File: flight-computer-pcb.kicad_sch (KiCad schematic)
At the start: 18 parts, among them J1 Battery, M1 Servo, U1 Teensy4.1, U10 U3V16F9, U2 BMP390, U3 BNO055, U4 Pressure Transducer, U5 Ultimate_GPS, U6 Parani-ESD100V2, U7 U3V70F6, U8 S7V8F3, U9 S13V10F5

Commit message: feat: add S13V10F5
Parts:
- U6: footprint FlightComputer:BNO055 -> (none)
- U9: footprint (none) -> FlightComputer:S13V10F5
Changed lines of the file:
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@@
 			)
 		)
-		(property "Footprint" "FlightComputer:BNO055"
+		(property "Footprint" ""
 			(at 233.68 115.57 0)
 			(effects
@@
 			)
 		)
-		(property "Footprint" ""
+		(property "Footprint" "FlightComputer:S13V10F5"
 			(at 125.73 170.18 0)
 			(effects

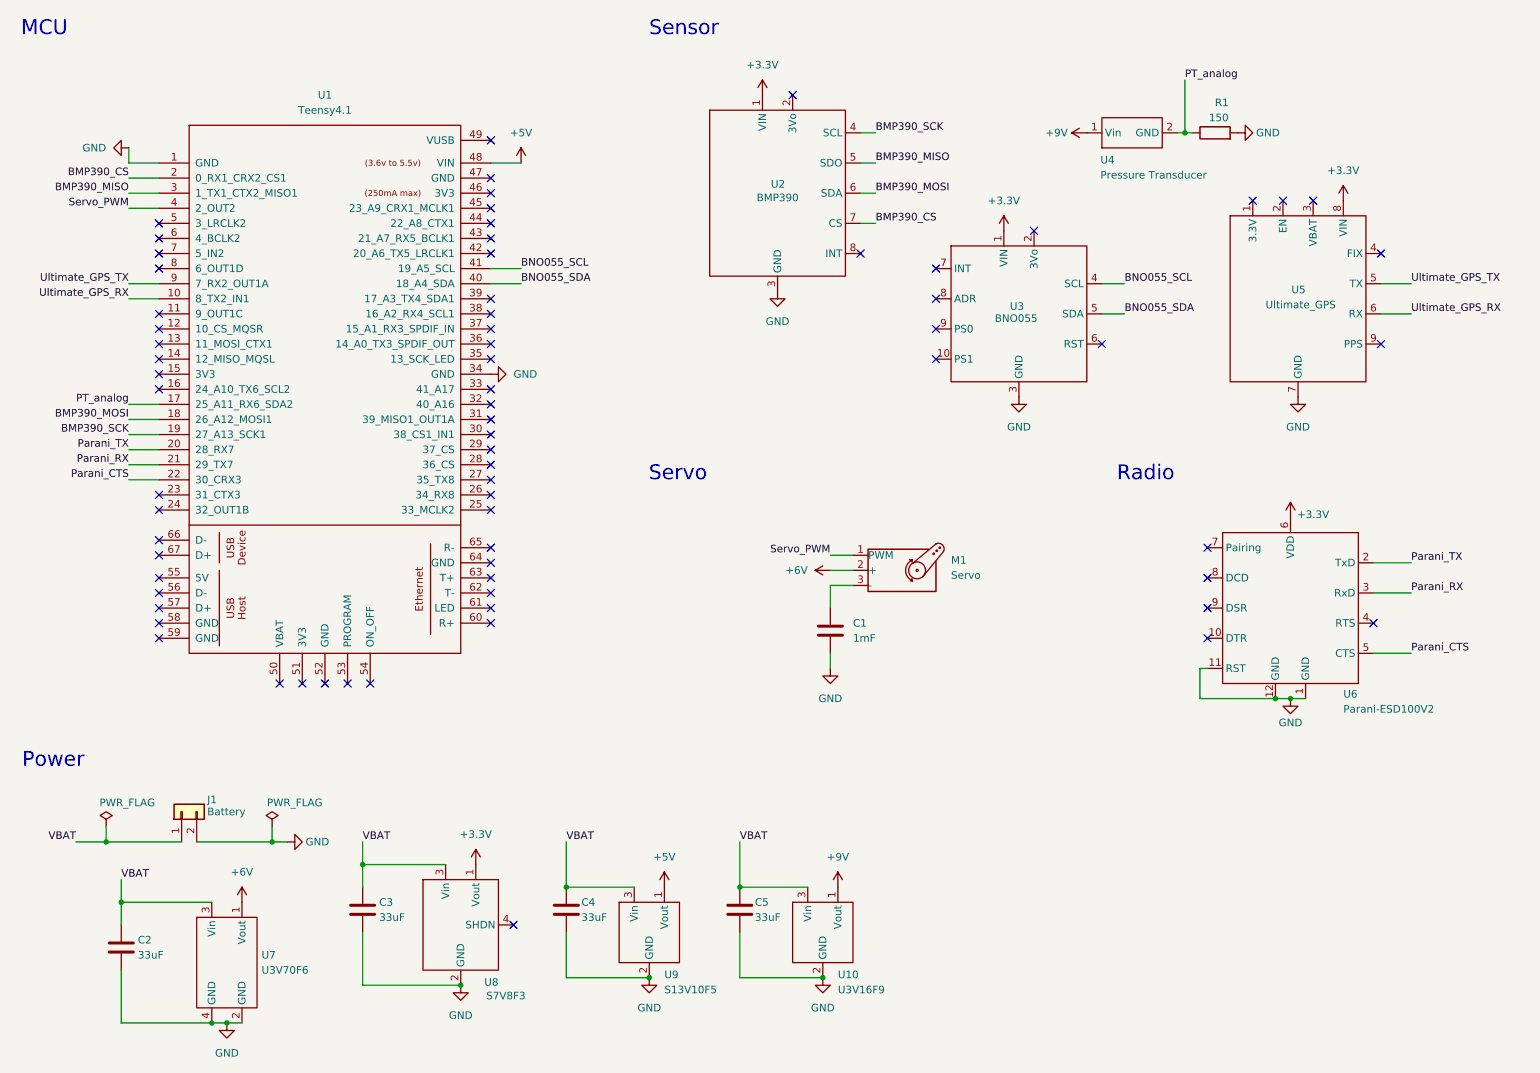
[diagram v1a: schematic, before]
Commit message: feat: add connectors to schematic
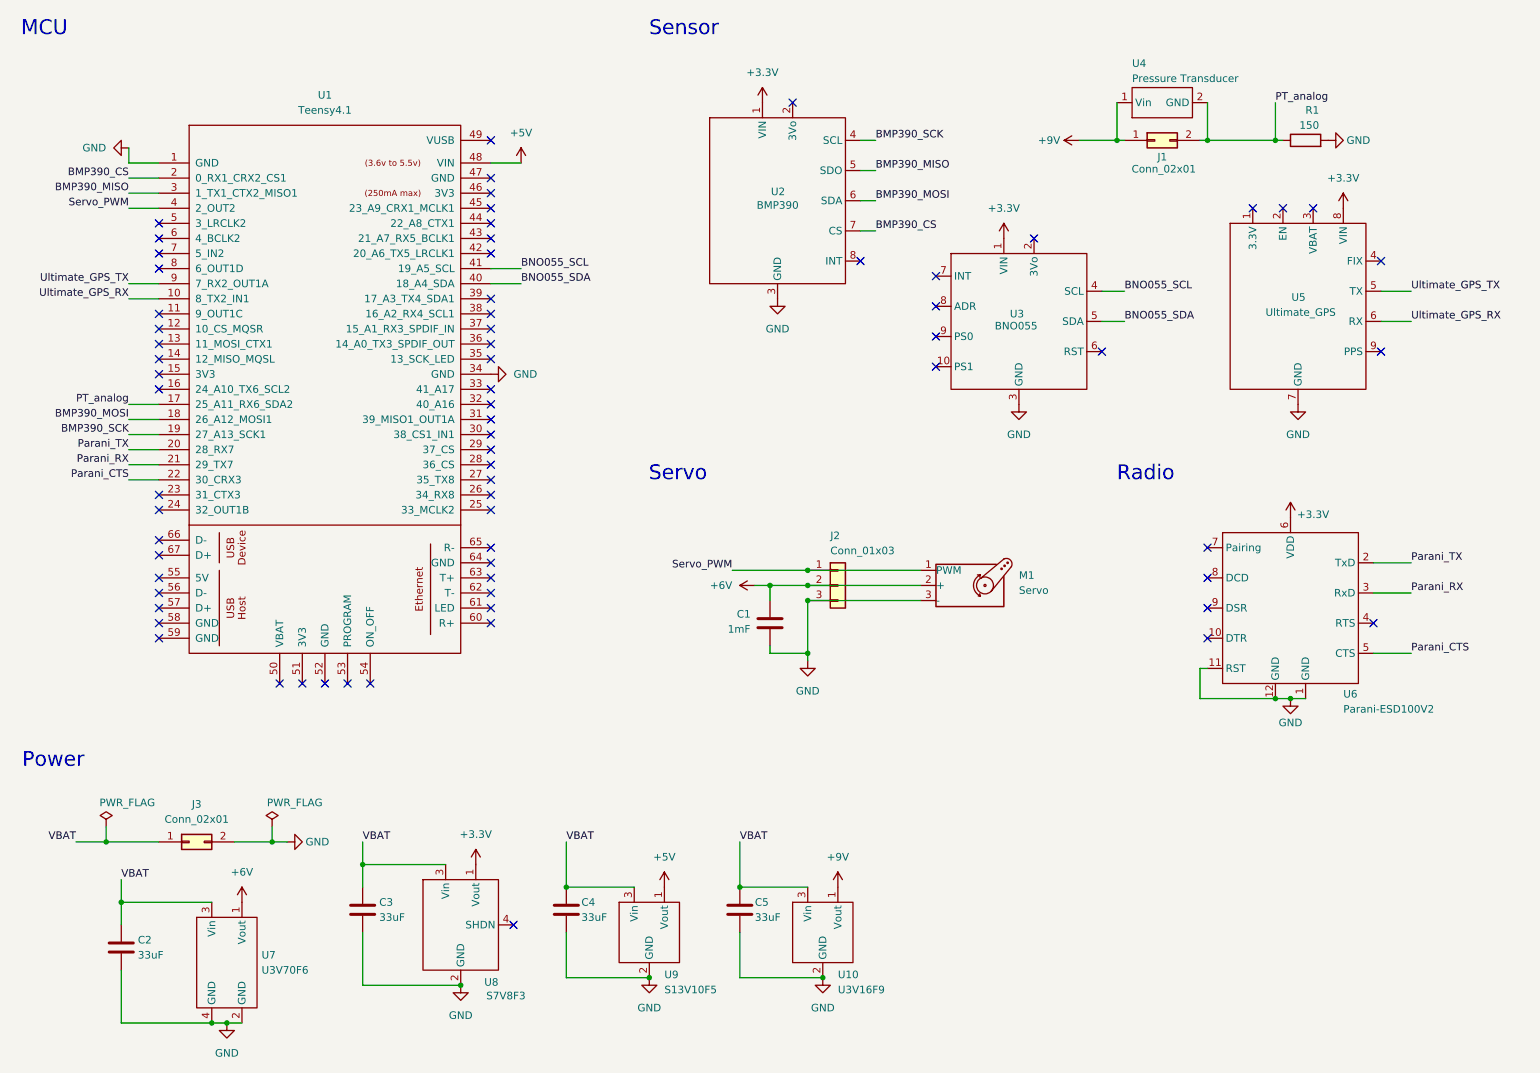
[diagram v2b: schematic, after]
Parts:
- removed J1: Battery, symbol Connector_Generic:Conn_01x02
- added J1, J3: Conn_02x01, symbol Connector_Generic:Conn_02x01
- added J2: Conn_01x03, symbol Connector_Generic:Conn_01x03
- M1, U4: now left out of the parts list
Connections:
- net +6V: now also C1.1, J2.2 (Pin_2)
- net +9V: now also J1.1 (Pin_1)
- net GND: now also M1.3 (-), J2.3 (Pin_3), J3.2 (Pin_2)
- net PT_analog: now also J1.2 (Pin_2)
- net Servo_PWM: now also J2.1 (Pin_1)
- net VBAT: now also J3.1 (Pin_1)
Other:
- moved on the sheet: C1, M1, R1, U2, U3, U4, U5

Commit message: docs: add "external module" comments to schematic
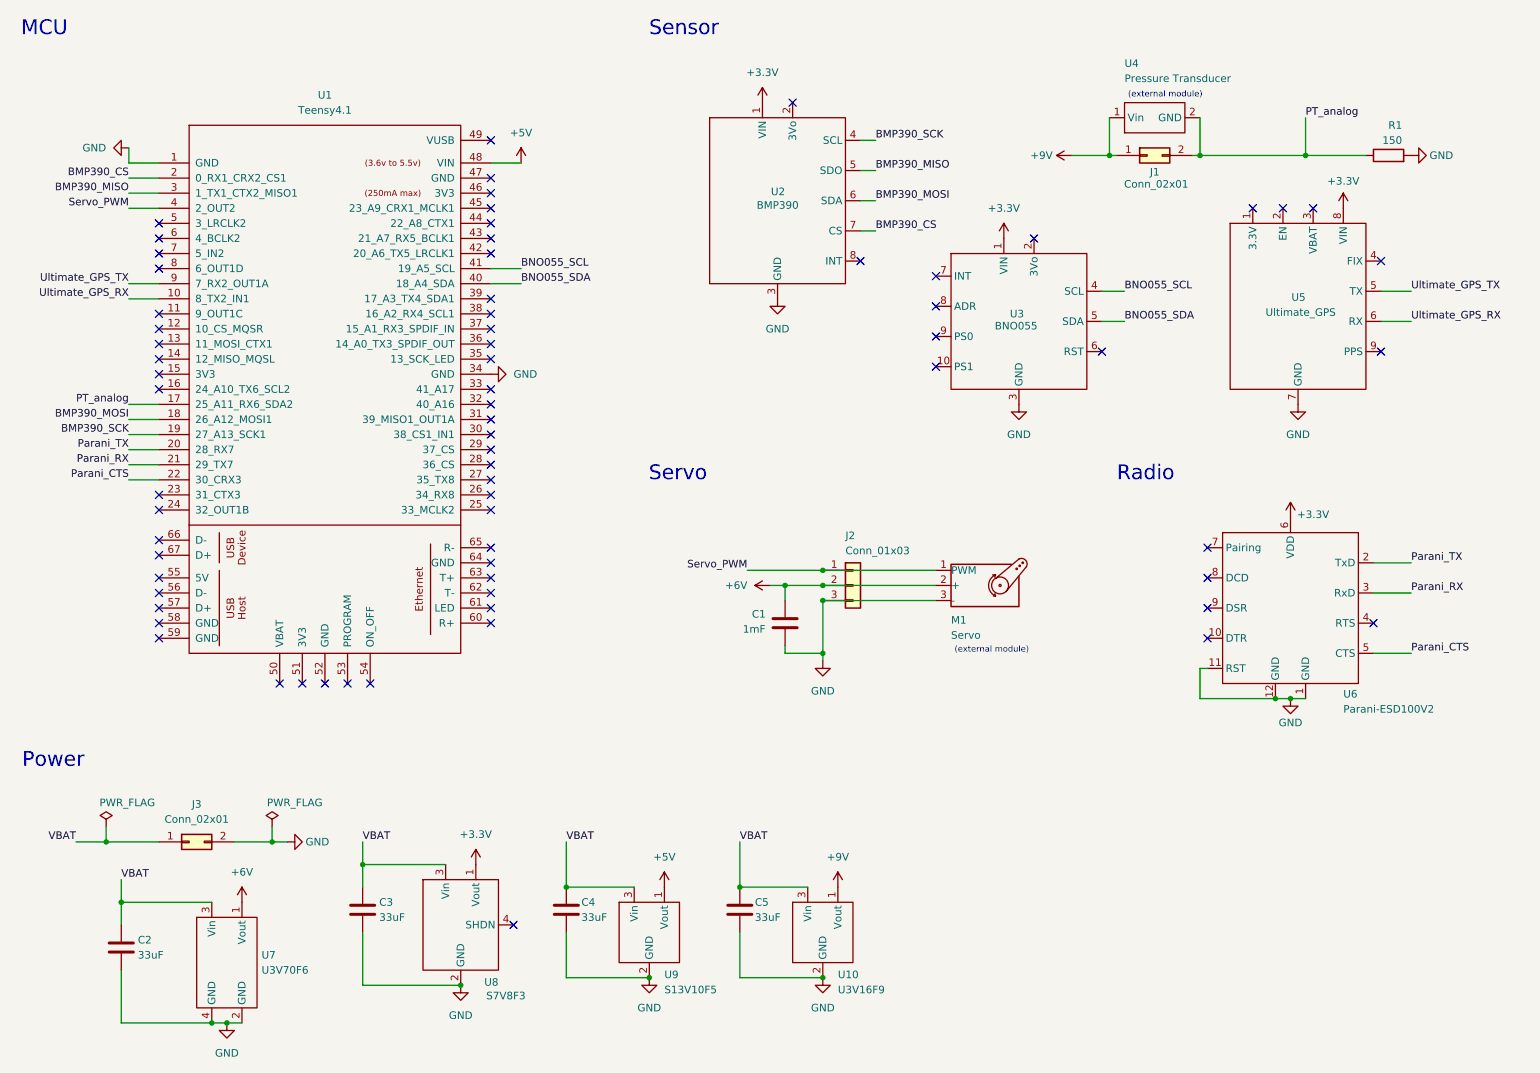
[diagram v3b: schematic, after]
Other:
- note added: "(external module)"
- moved on the sheet: C1, J1, J2, M1, R1, U4

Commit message: feat: add S7V8F3, U3V16F9, and U3V70F6 footprint to sch and pcb
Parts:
- U10: footprint (none) -> FlightComputer:U3V16F9
- U7: footprint (none) -> FlightComputer:U3V70F6
- U8: footprint (none) -> FlightComputer:S7V8F3
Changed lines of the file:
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@@
 			)
 		)
-		(property "Footprint" ""
+		(property "Footprint" "FlightComputer:U3V70F6"
 			(at 54.61 175.26 0)
 			(effects
@@
 			)
 		)
-		(property "Footprint" ""
+		(property "Footprint" "FlightComputer:U3V16F9"
 			(at 154.94 170.18 0)
 			(effects
@@
 			)
 		)
-		(property "Footprint" ""
+		(property "Footprint" "FlightComputer:S7V8F3"
 			(at 93.98 168.91 0)
 			(effects

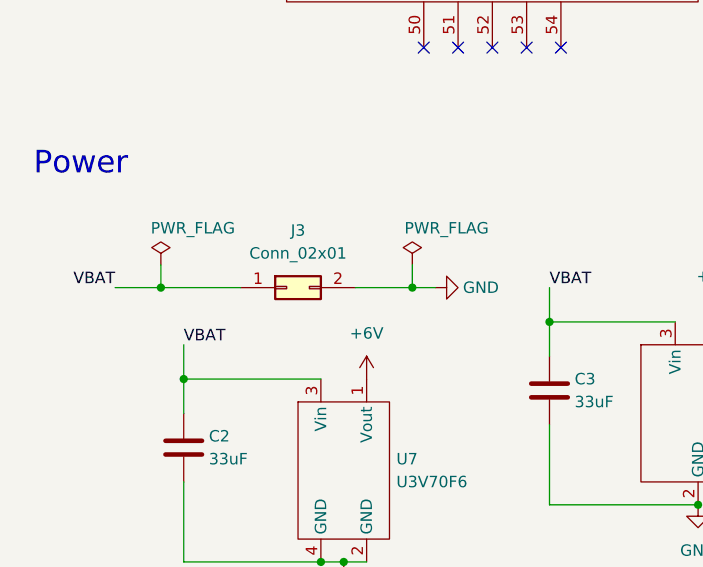
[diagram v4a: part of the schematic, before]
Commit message: feat: add connector footprints to J1, J2 and J3
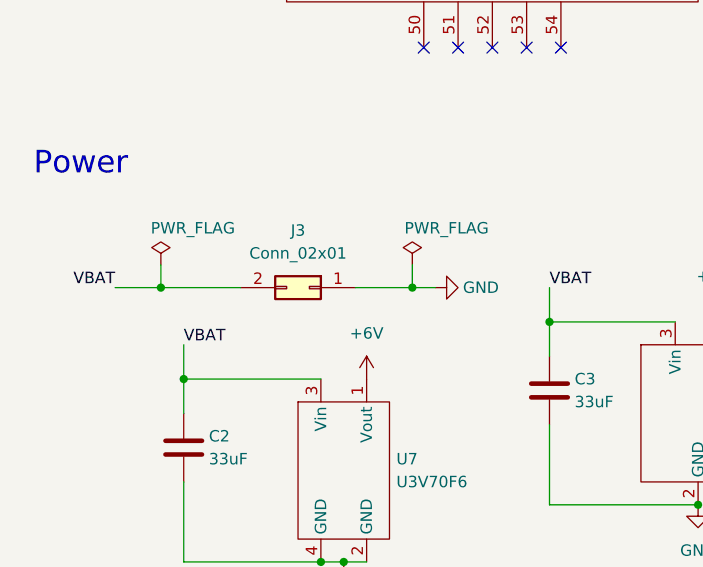
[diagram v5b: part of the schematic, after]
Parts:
- J1: footprint (none) -> Connector_JST:JST_XH_S2B-XH-A-1_1x02_P2.50mm_Horizontal
- J2: footprint (none) -> Connector_JST:JST_XH_S3B-XH-A-1_1x03_P2.50mm_Horizontal
- J3: footprint (none) -> Connector_AMASS:AMASS_XT30PW-M_1x02_P2.50mm_Horizontal
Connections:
- net GND: now also J3.1 (Pin_1); no longer J3.2 (Pin_2)
- net VBAT: now also J3.2 (Pin_2); no longer J3.1 (Pin_1)
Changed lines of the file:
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@@
 			)
 		)
-		(property "Footprint" ""
+		(property "Footprint" "Connector_JST:JST_XH_S2B-XH-A-1_1x02_P2.50mm_Horizontal"
 			(at 209.55 39.37 0)
 			(effects
@@
 	(symbol
 		(lib_id "Connector_Generic:Conn_02x01")
-		(at 48.26 154.94 0)
-		(unit 1)
-		(exclude_from_sim no)
-		(in_bom yes)
-		(on_board yes)
-		(dnp no)
-		(fields_autoplaced yes)
+		(at 50.8 154.94 0)
+		(mirror y)
+		(unit 1)
+		(exclude_from_sim no)
+		(in_bom yes)
+		(on_board yes)
+		(dnp no)
 		(property "Reference" "J3"
 			(at 49.53 148.59 0)
@@
 			)
 		)
-		(property "Footprint" ""
-			(at 48.26 154.94 0)
+		(property "Footprint" "Connector_AMASS:AMASS_XT30PW-M_1x02_P2.50mm_Horizontal"
+			(at 50.8 154.94 0)
 			(effects
 				(font
@@
 		)
 		(property "Datasheet" "~"
-			(at 48.26 154.94 0)
+			(at 50.8 154.94 0)
 			(effects
 				(font
@@
 		)
 		(property "Description" "Generic connector, double row, 02x01, this symbol is compatible with counter-clockwise, top-bottom and odd-even numbering schemes., script generated (kicad-library-utils/schlib/autogen/connector/)"
-			(at 48.26 154.94 0)
+			(at 50.8 154.94 0)
 			(effects
 				(font
@@
 			)
 		)
-		(property "Footprint" ""
+		(property "Footprint" "Connector_JST:JST_XH_S3B-XH-A-1_1x03_P2.50mm_Horizontal"
 			(at 160.02 111.76 0)
 			(effects
